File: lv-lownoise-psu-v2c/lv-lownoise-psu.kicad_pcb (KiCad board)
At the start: 2 copper layers, 71.1 x 61 mm, 48 parts, among them J1 AC, J10 GND, J11 GND, J12 -5V, J2 GND, J3 AC, J4 +15V, J5 GND, J6 -15V, J7 +5V, J8 GND, J9 LED, Q1 BD679, Q2 BD680, U1 LT1761-BYP, U2 LT1964-BYP, U3 L78L05_SOT89, U4 L79L05_SOT89

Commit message: finalize v2c version
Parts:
- added R10: 0R, Resistor_SMD:R_0805_2012Metric_Pad1.15x1.40mm_HandSolder, F.Cu at (121.7, 78.7)
- added R11: 0R, Resistor_SMD:R_0805_2012Metric_Pad1.15x1.40mm_HandSolder, F.Cu at (125.5, 78.7)
- added R4: 0R, Resistor_SMD:R_0805_2012Metric_Pad1.15x1.40mm_HandSolder, F.Cu at (121.4, 47.1)
- added R9: 0R, Resistor_SMD:R_0805_2012Metric_Pad1.15x1.40mm_HandSolder, F.Cu at (125.2, 47.1)
- C1, C2: value 4700uF -> 2200uF
- D1: value MB4S -> DF06M; footprint Package_TO_SOT_SMD:TO-269AA -> Diode_THT:Diode_Bridge_DIP-4_W7.62mm_P5.08mm
- moved C2 14.3 mm to (108.0, 69.3), turned to 270 degrees
- moved C14 13.5 mm to (124.6, 80.9), turned to 180 degrees
- moved C11 10.3 mm to (120.2, 45.0)
- moved U3 10.3 mm to (125.0, 43.5)
- moved C12 10.3 mm to (120.2, 42.0)
- moved U4 10.1 mm to (123.6, 84.7), turned to 270 degrees
- moved C15 8.54 mm to (120.5, 80.9), turned to 0 degrees
- moved C16 6.79 mm to (116.6, 87.9), turned to 0 degrees
- moved C1 5.75 mm to (108.0, 48.3)
- moved D1 4.40 mm to (97.0, 64.6), turned to 180 degrees
- moved C13 0.76 mm to (123.3, 37.0), turned to 90 degrees
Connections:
- C11 pad 1: Net-(C1-Pad1) -> Net-(C11-Pad1)
- C2 pad 2: Net-(C14-Pad2) -> Net-(C2-Pad2)
- D1 pad 1: Net-(D1-Pad1) -> Net-(C1-Pad1)
- D1 pad 2: Net-(D1-Pad2) -> Net-(C2-Pad2)
- D1 pad 3: Net-(C1-Pad1) -> Net-(D1-Pad3)
- D1 pad 4: Net-(C14-Pad2) -> Net-(D1-Pad4)
- J1 pad 1: Net-(D1-Pad2) -> Net-(D1-Pad4)
- J3 pad 1: Net-(D1-Pad1) -> Net-(D1-Pad3)
- Q2 pad 2: Net-(C14-Pad2) -> Net-(C2-Pad2)
- R8 pad 2: Net-(C14-Pad2) -> Net-(C2-Pad2)
- U3 pad 3: Net-(C1-Pad1) -> Net-(C11-Pad1)
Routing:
- net Net-(C14-Pad2): track 54.5 -> 6.22 mm, vias 2 -> 0
- net Net-(C2-Pad2): track 0.00 -> 43.6 mm
- net Net-(D1-Pad1): track 7.97 -> 0.00 mm, vias 1 -> 0
- net Net-(D1-Pad2): track 7.97 -> 0.00 mm, vias 1 -> 0
- net Net-(C12-Pad1): track 37.3 -> 30.4 mm
- net Net-(D1-Pad4): track 0.00 -> 6.47 mm
- net Net-(D1-Pad3): track 0.00 -> 6.22 mm
- net Net-(C11-Pad1): track 0.00 -> 5.97 mm
- net Net-(C4-Pad2): track 5.36 -> 9.37 mm
- net Net-(C15-Pad2): track 16.8 -> 20.7 mm
- net Net-(C3-Pad1): track 5.97 -> 9.10 mm
- net Net-(C1-Pad1): track 42.7 -> 44.2 mm, vias 2 -> 0
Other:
- board text added: "Low noise dual power supply V2c Michael Schenk, 2020.11.13"
- board text removed: "Low noise dual power supply V2c Michael Schenk, 2020.11.12"

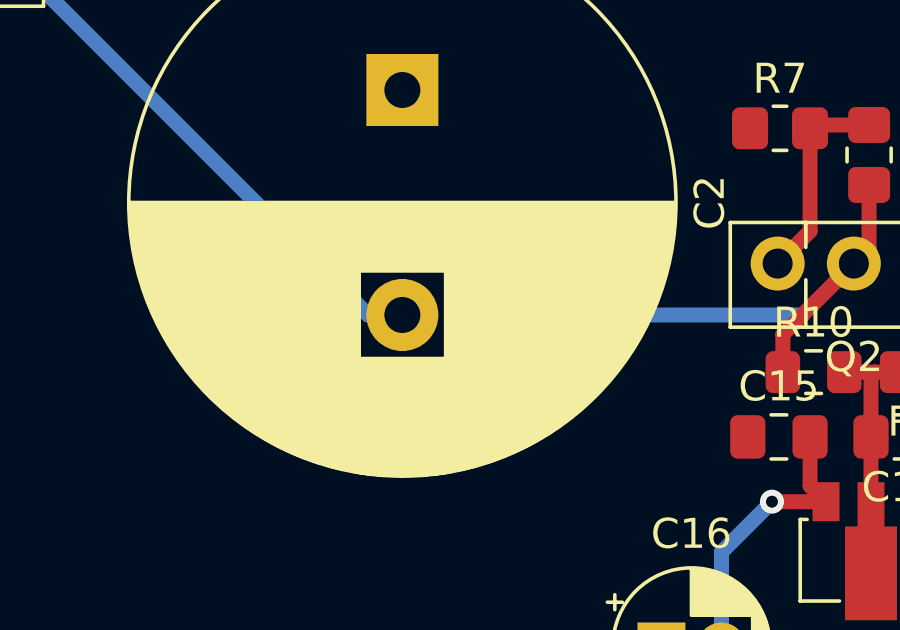
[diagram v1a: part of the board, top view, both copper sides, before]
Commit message: fix DRC error
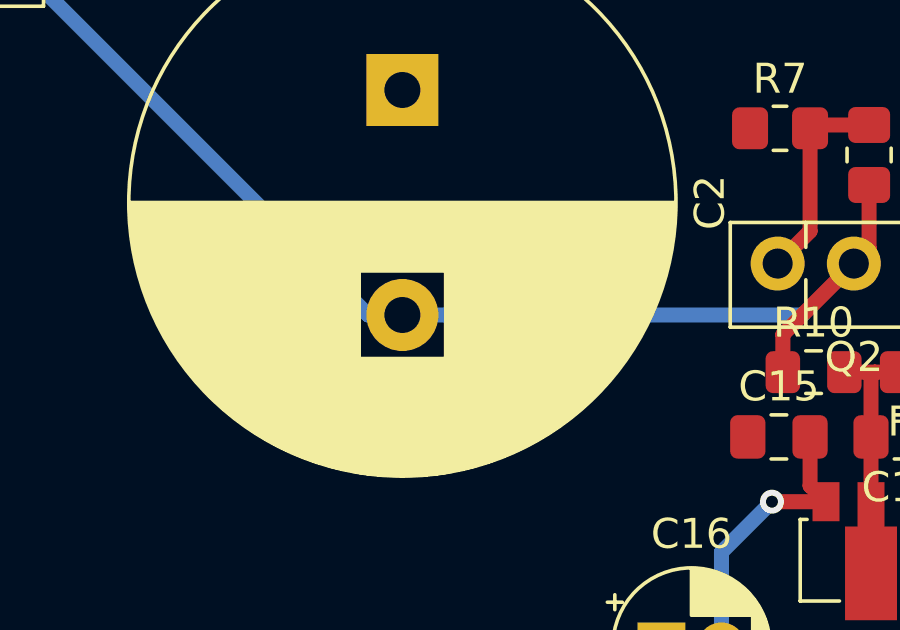
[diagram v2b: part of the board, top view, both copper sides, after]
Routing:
- net Net-(C2-Pad2): track 43.6 -> 46.8 mm

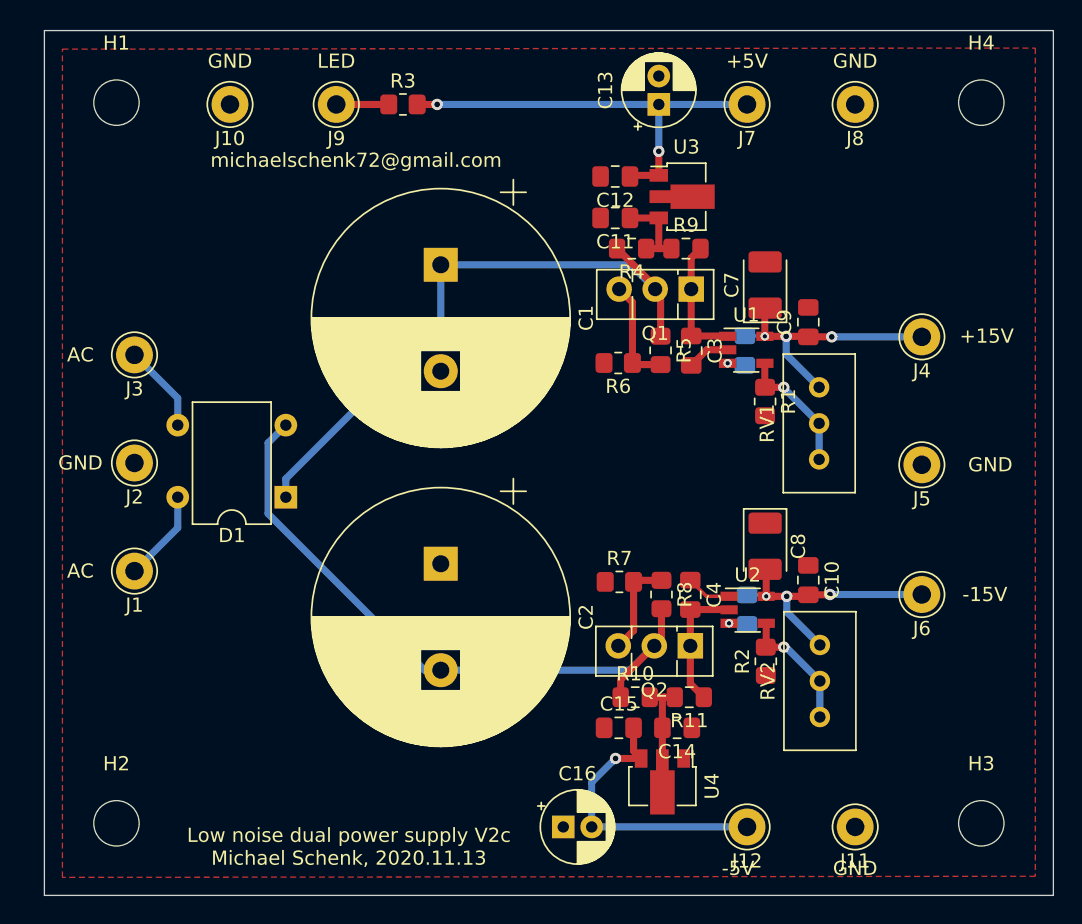
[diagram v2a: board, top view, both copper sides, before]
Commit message: fix 100uF footprint issue
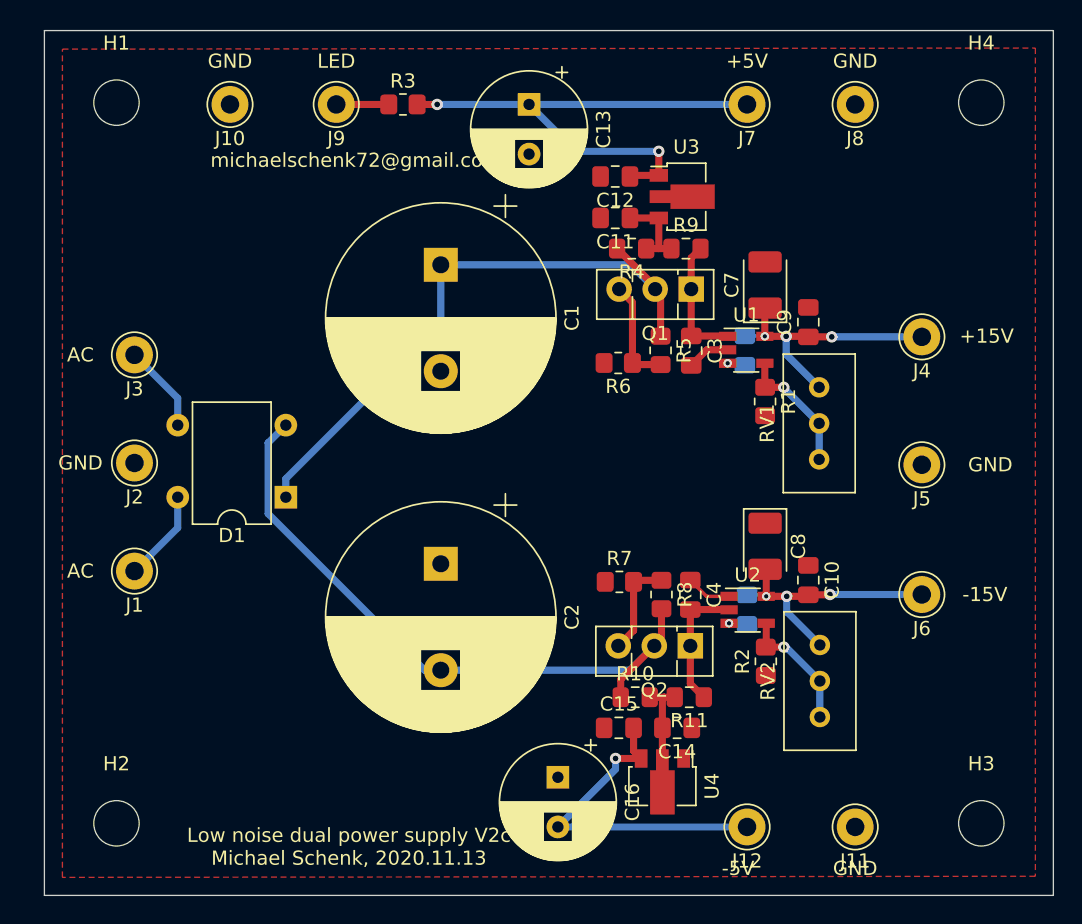
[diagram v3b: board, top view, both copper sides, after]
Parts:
- C1, C2: footprint Capacitor_THT:CP_Radial_D18.0mm_P7.50mm -> Capacitor_THT:CP_Radial_D16.0mm_P7.50mm
- C13, C16: footprint Capacitor_THT:CP_Radial_D5.0mm_P2.00mm -> Capacitor_THT:CP_Radial_D8.0mm_P3.50mm
- moved C13 9.14 mm to (114.2, 37.0), turned to 270 degrees
- moved C16 3.52 mm to (116.2, 84.4), turned to 270 degrees
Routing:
- net Net-(C12-Pad1): track 30.4 -> 37.6 mm
- net Net-(C15-Pad2): track 20.7 -> 24.0 mm

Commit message: adapt pre-regulator voltage divider
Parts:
- R5, R8: value 1k -> 3.16k
- R6, R7: value 16k -> 21k
